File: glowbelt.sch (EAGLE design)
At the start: 12 parts, among them IC1 TINY10S

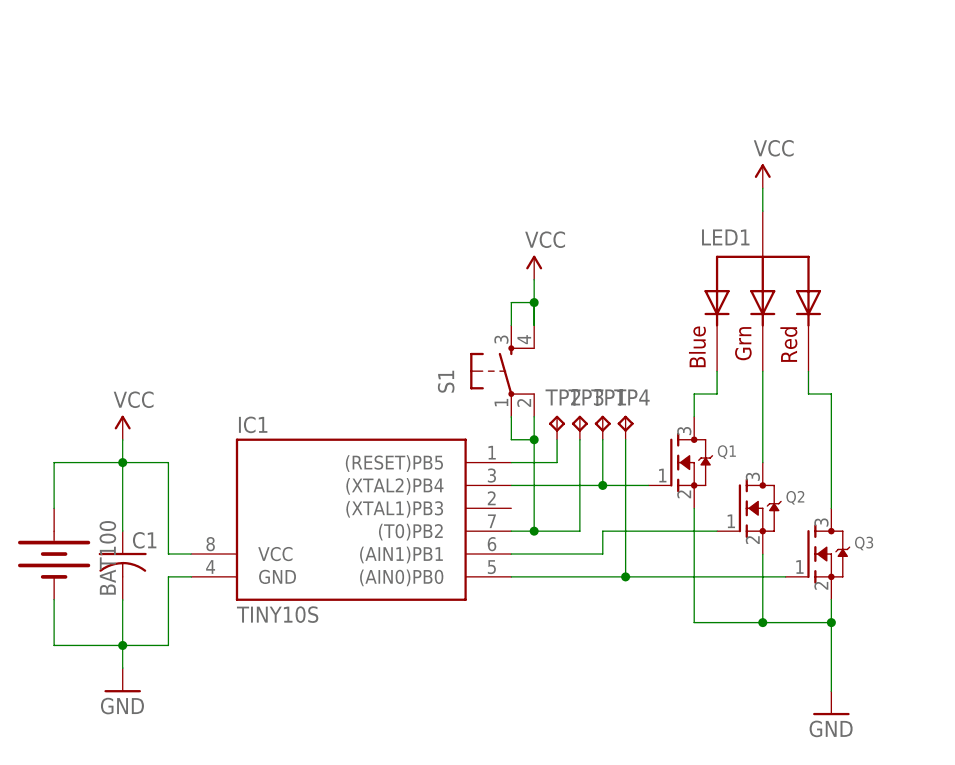
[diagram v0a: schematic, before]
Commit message: added optional current limiting resistor array
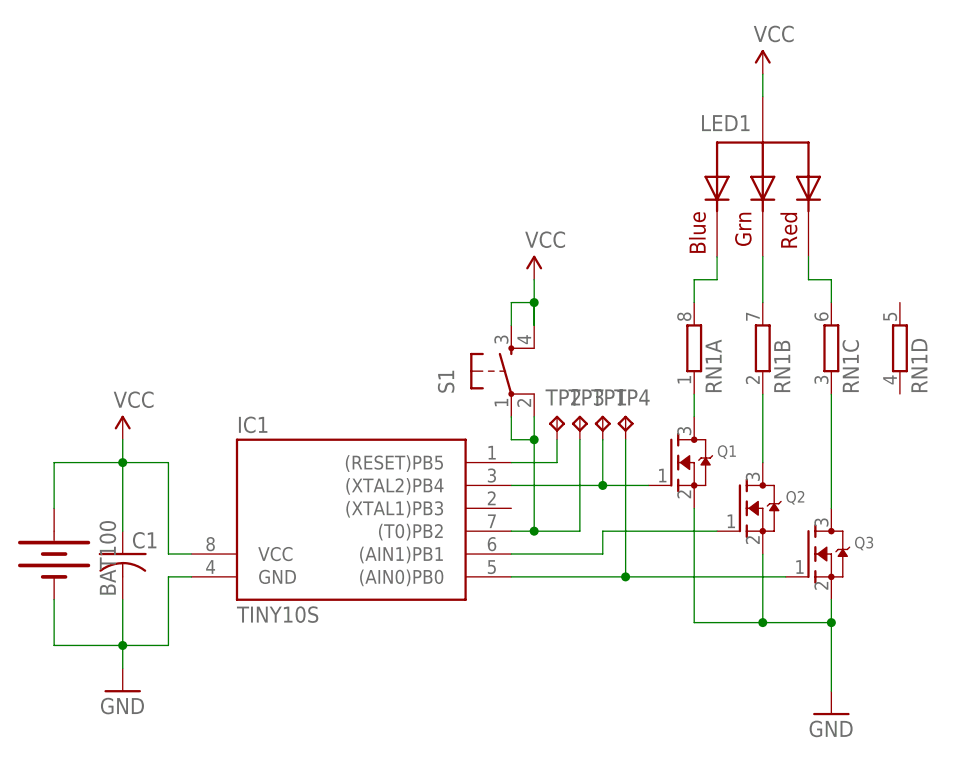
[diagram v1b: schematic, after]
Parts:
- added RN1: (no value), resistor-dil:4R-NEXBS8V
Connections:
- removed net N$10: LED1.RED, Q3.D
- removed net N$8: LED1.BLUE, Q1.D
- removed net N$9: LED1.GREEN, Q2.D
- new net N$2: Q1.D, RN1A.1
- new net N$3: Q2.D, RN1B.1
- new net N$4: Q3.D, RN1C.1
- new net N$5: LED1.GREEN, RN1B.2
- new net N$6: LED1.BLUE, RN1A.2
- new net N$7: LED1.RED, RN1C.2
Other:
- moved on the sheet: LED1
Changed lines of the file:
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@@
 <part name="P+4" library="sparkfun" deviceset="VCC" device=""/>
 <part name="LED1" library="adafruit" deviceset="RGBLED_CA" device="-5MM"/>
+<part name="RN1" library="resistor-dil" deviceset="4R-N" device="EXBS8V"/>
 </parts>
 <sheets>
@@
 <instance part="S1" gate="S" x="91.44" y="81.28" rot="R90"/>
 <instance part="P+3" gate="1" x="93.98" y="91.44"/>
-<instance part="P+4" gate="1" x="119.38" y="101.6"/>
-<instance part="LED1" gate="G$1" x="119.38" y="88.9" rot="MR270"/>
+<instance part="P+4" gate="1" x="119.38" y="114.3"/>
+<instance part="LED1" gate="G$1" x="119.38" y="101.6" rot="MR270"/>
+<instance part="RN1" gate="A" x="111.76" y="83.82" rot="R90"/>
+<instance part="RN1" gate="B" x="119.38" y="83.82" rot="R90"/>
+<instance part="RN1" gate="C" x="127" y="83.82" rot="R90"/>
+<instance part="RN1" gate="D" x="134.62" y="83.82" rot="R90"/>
 </instances>
 <busses>
@@
 <pinref part="LED1" gate="G$1" pin="VCC"/>
 <pinref part="P+4" gate="1" pin="VCC"/>
-<wire x1="119.38" y1="99.06" x2="119.38" y2="101.6" width="0.1524" layer="91"/>
+<wire x1="119.38" y1="111.76" x2="119.38" y2="114.3" width="0.1524" layer="91"/>
 </segment>
 </net>
@@
 </segment>
 </net>
-<net name="N$8" class="0">
-<segment>
-<pinref part="Q1" gate="G$1" pin="D"/>
-<wire x1="114.3" y1="81.28" x2="114.3" y2="78.74" width="0.1524" layer="91"/>
-<wire x1="114.3" y1="78.74" x2="111.76" y2="78.74" width="0.1524" layer="91"/>
-<wire x1="111.76" y1="78.74" x2="111.76" y2="76.2" width="0.1524" layer="91"/>
-<pinref part="LED1" gate="G$1" pin="BLUE"/>
-</segment>
-</net>
-<net name="N$9" class="0">
-<segment>
-<pinref part="Q2" gate="G$1" pin="D"/>
-<wire x1="119.38" y1="81.28" x2="119.38" y2="71.12" width="0.1524" layer="91"/>
-<pinref part="LED1" gate="G$1" pin="GREEN"/>
-</segment>
-</net>
-<net name="N$10" class="0">
-<segment>
-<pinref part="Q3" gate="G$1" pin="D"/>
-<wire x1="124.46" y1="81.28" x2="124.46" y2="78.74" width="0.1524" layer="91"/>
-<wire x1="124.46" y1="78.74" x2="127" y2="78.74" width="0.1524" layer="91"/>
-<wire x1="127" y1="78.74" x2="127" y2="66.04" width="0.1524" layer="91"/>
-<pinref part="LED1" gate="G$1" pin="RED"/>
-</segment>
-</net>
 <net name="N$1" class="0">
 <segment>
@@
 </segment>
 </net>
+<net name="N$2" class="0">
+<segment>
+<pinref part="Q1" gate="G$1" pin="D"/>
+<pinref part="RN1" gate="A" pin="1"/>
+<wire x1="111.76" y1="78.74" x2="111.76" y2="76.2" width="0.1524" layer="91"/>
+</segment>
+</net>
+<net name="N$3" class="0">
+<segment>
+<pinref part="Q2" gate="G$1" pin="D"/>
+<pinref part="RN1" gate="B" pin="1"/>
+<wire x1="119.38" y1="78.74" x2="119.38" y2="71.12" width="0.1524" layer="91"/>
+</segment>
+</net>
+<net name="N$4" class="0">
+<segment>
+<pinref part="Q3" gate="G$1" pin="D"/>
+<pinref part="RN1" gate="C" pin="1"/>
+<wire x1="127" y1="78.74" x2="127" y2="66.04" width="0.1524" layer="91"/>
+</segment>
+</net>
+<net name="N$5" class="0">
+<segment>
+<pinref part="RN1" gate="B" pin="2"/>
+<pinref part="LED1" gate="G$1" pin="GREEN"/>
+<wire x1="119.38" y1="93.98" x2="119.38" y2="88.9" width="0.1524" layer="91"/>
+</segment>
+</net>
+<net name="N$6" class="0">
+<segment>
+<pinref part="RN1" gate="A" pin="2"/>
+<pinref part="LED1" gate="G$1" pin="BLUE"/>
+<wire x1="114.3" y1="93.98" x2="114.3" y2="91.44" width="0.1524" layer="91"/>
+<wire x1="114.3" y1="91.44" x2="111.76" y2="91.44" width="0.1524" layer="91"/>
+<wire x1="111.76" y1="91.44" x2="111.76" y2="88.9" width="0.1524" layer="91"/>
+</segment>
+</net>
+<net name="N$7" class="0">
+<segment>
+<pinref part="RN1" gate="C" pin="2"/>
+<pinref part="LED1" gate="G$1" pin="RED"/>
+<wire x1="124.46" y1="93.98" x2="124.46" y2="91.44" width="0.1524" layer="91"/>
+<wire x1="124.46" y1="91.44" x2="127" y2="91.44" width="0.1524" layer="91"/>
+<wire x1="127" y1="91.44" x2="127" y2="88.9" width="0.1524" layer="91"/>
+</segment>
+</net>
